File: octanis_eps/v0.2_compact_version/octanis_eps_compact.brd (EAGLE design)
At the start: 100 x 67.3 mm, 100 parts, among them IC3 OPA2333DGK, IC5 OPA2333DGK, IC6 OPA2333DGK, IC7 OPA2333DGK, IC9 OPA2333DGK, Q1 FC-12M

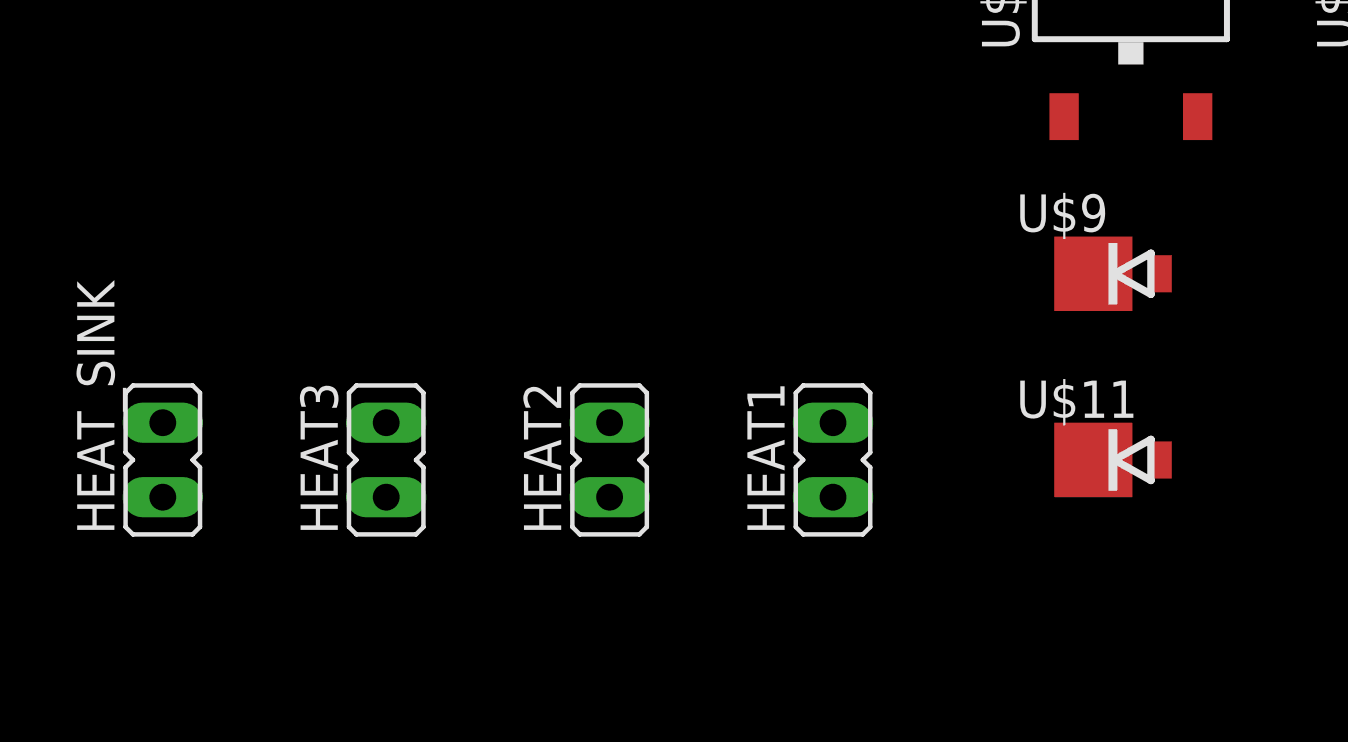
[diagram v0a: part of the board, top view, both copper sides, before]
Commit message: corrected zener connection error
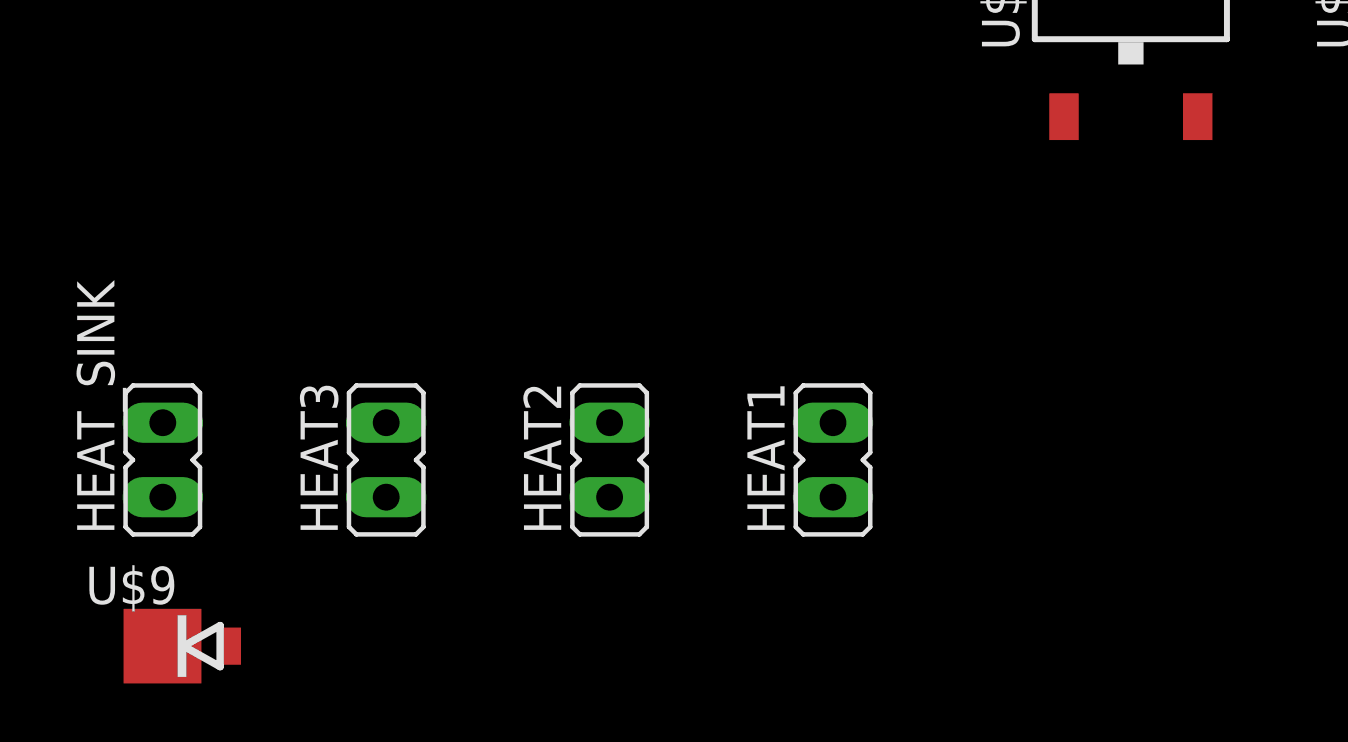
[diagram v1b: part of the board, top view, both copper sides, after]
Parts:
- removed U$11: MBRM120LTIG, Octanis1_EPS:DO216AA
- moved U$9 34.2 mm to (-104.1, -184.2)
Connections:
- removed net DISSIP1: IC9.2, U$11.A, U$7.3
- removed net DISSIP2: IC9.6, U$6.3, U$9.A
- net DISSIP: now also IC9.2, IC9.6, U$6.3, U$7.3, U$9.A; no longer U$11.C
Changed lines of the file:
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@@
 <element name="U$20" library="Octanis1_EPS" package="TO252" value="IRFR3711ZTRPBF" x="-59.69" y="-161.29"/>
 <element name="U$21" library="Octanis1_EPS" package="TO252" value="IRFR3711ZTRPBF" x="-71.12" y="-161.29"/>
-<element name="U$9" library="Octanis1_EPS" package="DO216AA" value="MBRM120LTIG" x="-72.39" y="-171.45"/>
-<element name="U$11" library="Octanis1_EPS" package="DO216AA" value="MBRM120LTIG" x="-72.39" y="-177.8"/>
 <element name="HEAT1" library="jumper" package="JP1" value="" x="-81.28" y="-177.8"/>
 <element name="HEAT2" library="jumper" package="JP1" value="" x="-88.9" y="-177.8"/>
 <element name="HEAT3" library="jumper" package="JP1" value="" x="-96.52" y="-177.8"/>
 <element name="HEAT_SINK" library="jumper" package="JP1" value="" x="-104.14" y="-177.8"/>
+<element name="U$9" library="Octanis1_EPS" package="DO216AA" value="MBRM120LTIG" x="-104.14" y="-184.15"/>
 </elements>
 <signals>
@@
 <wire x1="0.85" y1="-6.35" x2="-4.079240625" y2="-74.8284" width="0" layer="19" extent="1-1"/>
 </signal>
-<signal name="DISSIP1">
-<contactref element="IC9" pad="2"/>
-<contactref element="U$7" pad="3"/>
-<contactref element="U$11" pad="A"/>
-<wire x1="7.294" y1="15.667" x2="-70.0405" y2="-177.8" width="0" layer="19" extent="1-1"/>
-<wire x1="6.35" y1="17.82" x2="7.294" y2="15.667" width="0" layer="19" extent="1-16"/>
-</signal>
-<signal name="DISSIP2">
-<contactref element="U$6" pad="3"/>
-<contactref element="IC9" pad="6"/>
-<contactref element="U$9" pad="A"/>
-<wire x1="-12.7" y1="-82.59" x2="-70.0405" y2="-171.45" width="0" layer="19" extent="1-1"/>
-<wire x1="7.944" y1="19.892" x2="-12.7" y2="-82.59" width="0" layer="19" extent="1-1"/>
-</signal>
 <signal name="N$30">
 <contactref element="IC9" pad="7"/>
@@
 </signal>
 <signal name="DISSIP">
-<contactref element="U$11" pad="C"/>
-<contactref element="U$9" pad="C"/>
 <contactref element="U$8" pad="C"/>
 <contactref element="U$21" pad="2"/>
@@
 <contactref element="U$12" pad="2"/>
 <contactref element="HEAT_SINK" pad="2"/>
-<wire x1="-72.4" y1="-171.45" x2="-72.4" y2="-177.8" width="0" layer="19" extent="1-1"/>
-<wire x1="-68.84" y1="-166.09" x2="-72.4" y2="-171.45" width="0" layer="19" extent="1-1"/>
+<contactref element="U$6" pad="3"/>
+<contactref element="IC9" pad="6"/>
+<contactref element="IC9" pad="2"/>
+<contactref element="U$7" pad="3"/>
+<contactref element="U$9" pad="C"/>
+<contactref element="U$9" pad="A"/>
 <wire x1="-57.41" y1="-166.09" x2="-68.84" y2="-166.09" width="0" layer="19" extent="1-1"/>
 <wire x1="-45.98" y1="-166.09" x2="-57.41" y2="-166.09" width="0" layer="19" extent="1-1"/>
 <wire x1="-38.11" y1="-139.7" x2="-45.98" y2="-166.09" width="0" layer="19" extent="1-1"/>
-<wire x1="-104.14" y1="-176.53" x2="-72.4" y2="-177.8" width="0" layer="19" extent="1-1"/>
+<wire x1="-104.14" y1="-176.53" x2="-68.84" y2="-166.09" width="0" layer="19" extent="1-1"/>
+<wire x1="-104.15" y1="-184.15" x2="-104.14" y2="-176.53" width="0" layer="19" extent="1-1"/>
+<wire x1="-101.7905" y1="-184.15" x2="-104.15" y2="-184.15" width="0" layer="19" extent="1-1"/>
+<wire x1="-12.7" y1="-82.59" x2="-38.11" y2="-139.7" width="0" layer="19" extent="1-1"/>
+<wire x1="7.294" y1="15.667" x2="-12.7" y2="-82.59" width="0" layer="19" extent="1-1"/>
+<wire x1="6.35" y1="17.82" x2="7.294" y2="15.667" width="0" layer="19" extent="1-16"/>
+<wire x1="7.944" y1="19.892" x2="6.35" y2="17.82" width="0" layer="19" extent="1-16"/>
 </signal>
 <signal name="HEAT3">
